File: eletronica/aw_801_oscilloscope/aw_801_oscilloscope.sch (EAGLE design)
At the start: 56 parts, among them IC1 ICL7660CPA, IC2 ATMEGA162, IC4 LM4558N, Q2 16Mhz, X1 ANALOG, X2 USB, X3 DIG, X4 PROG

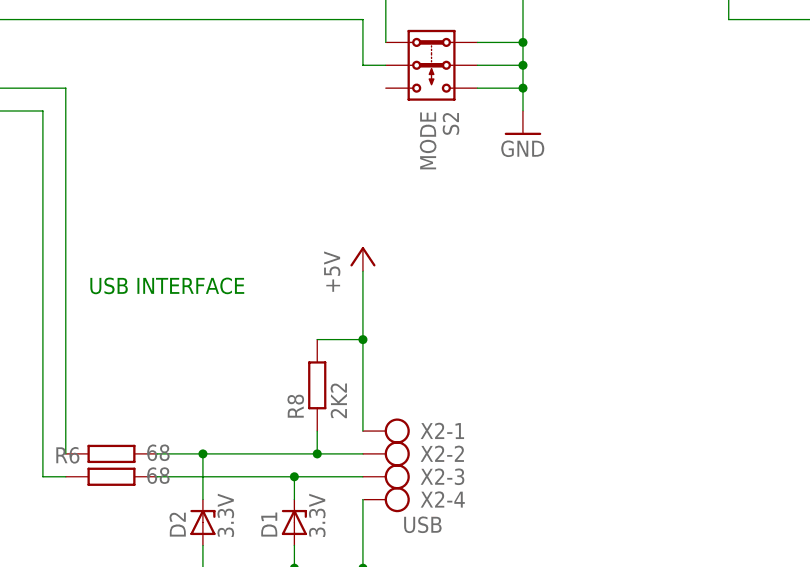
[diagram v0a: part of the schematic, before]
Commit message: 
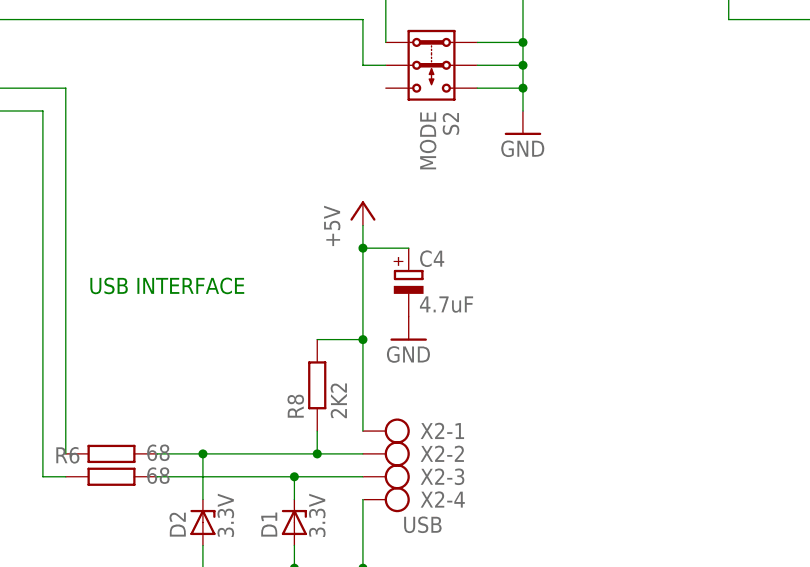
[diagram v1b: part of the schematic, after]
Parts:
- added C4: 4.7uF, rcl:CPOL-EUE2.5-6
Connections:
- net +5V: now also C4.+
- net GND: now also C4.-
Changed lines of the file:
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@@
 <part name="X4" library="con-ptr500" deviceset="AK300/6" device="" value="PROG"/>
 <part name="S4" library="switch" deviceset="MS243" device="" value="AN/DIG"/>
+<part name="C4" library="rcl" deviceset="CPOL-EU" device="E2.5-6" value="4.7uF"/>
+<part name="GND8" library="supply1" deviceset="GND" device=""/>
 </parts>
 <sheets>
@@
 <instance part="P+2" gate="1" x="48.26" y="175.26"/>
 <instance part="P+1" gate="1" x="198.12" y="251.46"/>
-<instance part="P+3" gate="1" x="139.7" y="58.42"/>
+<instance part="P+3" gate="1" x="139.7" y="63.5"/>
 <instance part="C3" gate="G$1" x="48.26" y="129.54"/>
 <instance part="D13" gate="G$1" x="99.06" y="228.6" rot="R90"/>
@@
 <instance part="X4" gate="-6" x="104.14" y="137.16" rot="R180"/>
 <instance part="S4" gate="1" x="121.92" y="93.98" rot="MR270"/>
+<instance part="C4" gate="G$1" x="144.78" y="55.88"/>
+<instance part="GND8" gate="1" x="144.78" y="48.26"/>
 </instances>
 <busses>
@@
 <junction x="48.26" y="121.92"/>
 </segment>
+<segment>
+<pinref part="C4" gate="G$1" pin="-"/>
+<pinref part="GND8" gate="1" pin="GND"/>
+</segment>
 </net>
 <net name="N$7" class="0">
@@
 <pinref part="P+3" gate="1" pin="+5V"/>
 <pinref part="R8" gate="G$1" pin="2"/>
-<wire x1="139.7" y1="48.26" x2="139.7" y2="55.88" width="0.1524" layer="91"/>
+<wire x1="139.7" y1="48.26" x2="139.7" y2="58.42" width="0.1524" layer="91"/>
+<wire x1="139.7" y1="58.42" x2="139.7" y2="60.96" width="0.1524" layer="91"/>
 <wire x1="134.62" y1="48.26" x2="139.7" y2="48.26" width="0.1524" layer="91"/>
 <junction x="139.7" y="48.26"/>
-</segment>
-<segment>
+<pinref part="C4" gate="G$1" pin="+"/>
+<wire x1="144.78" y1="58.42" x2="139.7" y2="58.42" width="0.1524" layer="91"/>
+<junction x="139.7" y="58.42"/>
+</segment>
+<segment>

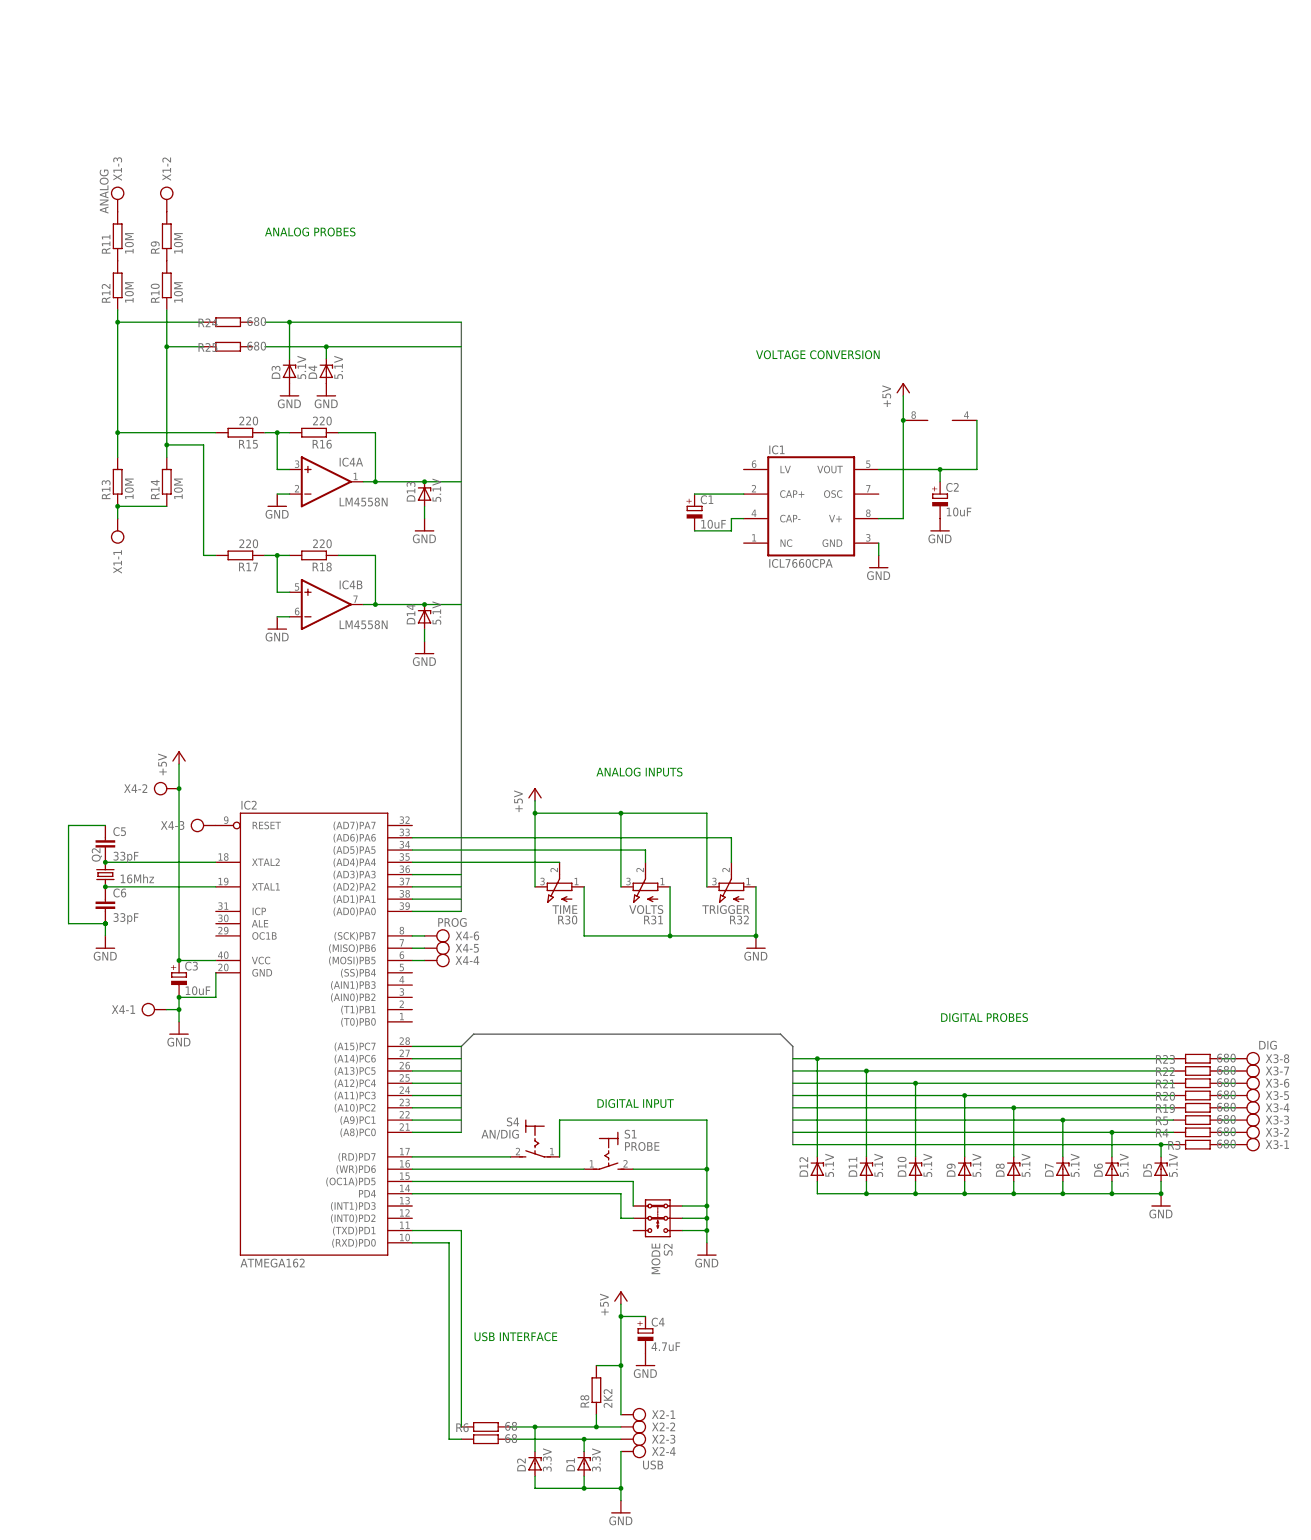
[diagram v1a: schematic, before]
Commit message: 
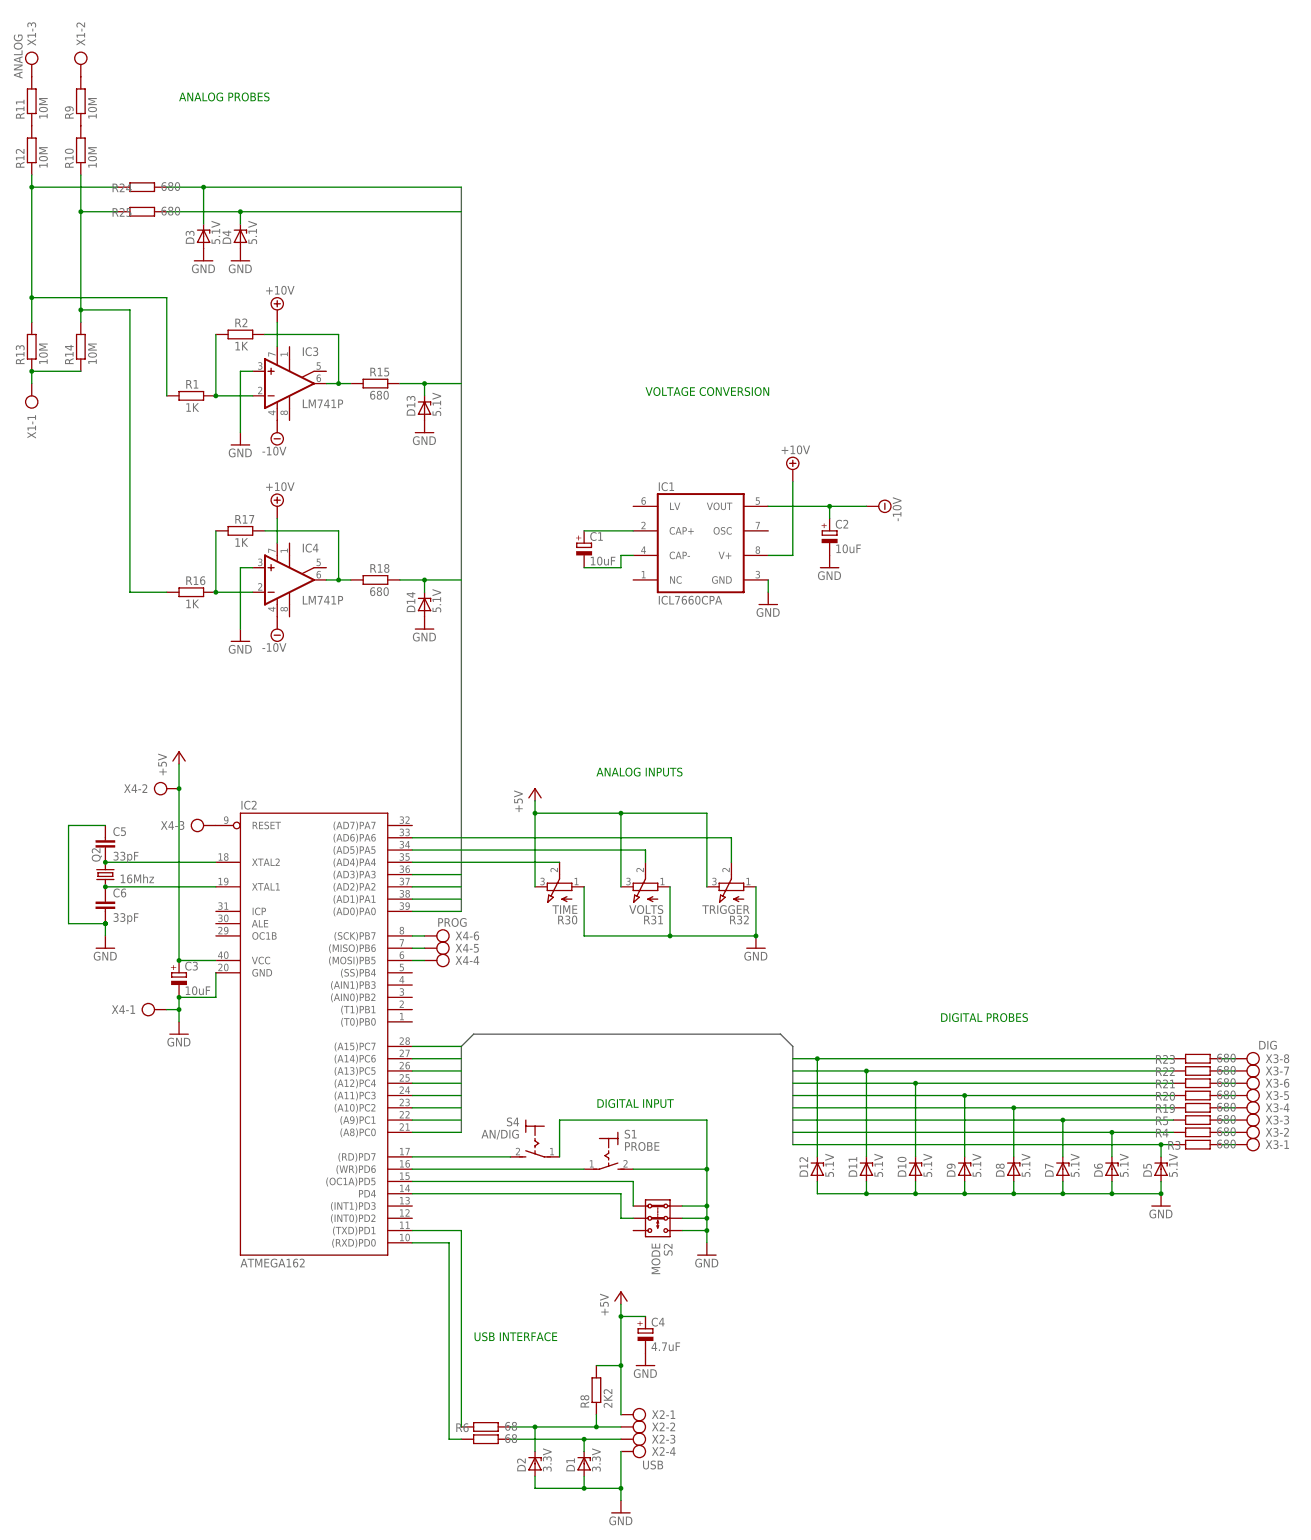
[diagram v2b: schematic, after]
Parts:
- added IC3: LM741P, linear:LM741P
- added R1, R2: 1K, rcl:R-EU_0207/10
- IC4: value LM4558N -> LM741P; device linear:LM4558N -> linear:LM741P
- R15, R18: value 220 -> 680
- R16, R17: value 220 -> 1K
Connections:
- removed net VOUT: C2.+, IC1.VOUT, IC4P.V-
- new net +10V: IC1.V+, IC3.V+, IC4.V+
- new net -10V: C2.+, IC1.VOUT, IC3.V-, IC4.V-
- new net N$35: IC3.OUT, R15.1, R2.2
- new net N$38: IC4.OUT, R17.2, R18.1
- net +5V: no longer IC1.V+, IC4P.V+
- net ANALOG0: now also R24.2
- net ANALOG1: now also R25.2
- net ANALOG2: now also R15.2; no longer IC4A.OUT, R16.1
- net ANALOG3: now also R18.2; no longer IC4B.OUT, R18.1
- net GND: now also IC3.+IN, IC4.+IN; no longer IC4A.-IN, IC4B.-IN
- net N$1: now also R1.1; no longer R15.2
- net N$16: now also R16.1; no longer R17.2
- net N$17: now also IC3.-IN, R1.2, R2.1; no longer IC4A.+IN, R15.1, R16.2
- net N$19: now also IC4.-IN, R16.2; no longer IC4B.+IN, R18.2
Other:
- moved on the sheet: C1, C2, D13, D14, D3, D4, IC1, R10, R11, R12, R13, R14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
